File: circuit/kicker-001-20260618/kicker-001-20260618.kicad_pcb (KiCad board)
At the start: 2 copper layers, 71.4 x 59.3 mm, 60 parts, among them J1 Solenoid_{Stroke}, J2 Solenoid_{Chip}, J3 Drribler_{Front}, J4 Conn_Relay, J6 Voltmeter, Q1 BSS138, Q2 TJ15S06M3L, Q3 Q_Photo_CE, Q4 MTB010N06RJ3, Q5 MTB010N06RJ3, U1 NOT, U10 TLP2361, U11 AND, U12 AND, U2 TLP2361, U3 XL6009E1, U4 NOT, U5 NOT, U6 DRV8874, U7 NOT, U8 NOT, U9 TLP2361

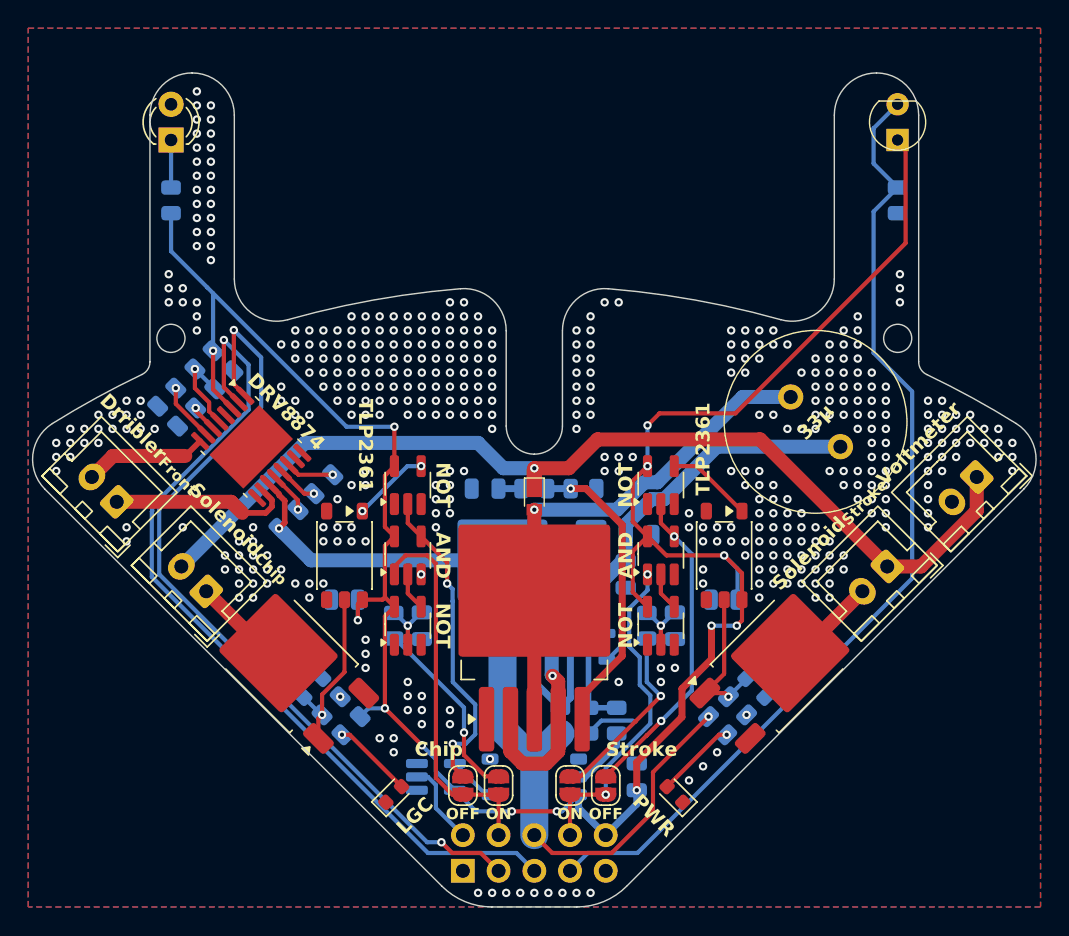
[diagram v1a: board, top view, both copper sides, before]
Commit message: Update キッカー基板のピンソケット→ピンヘッダ変更
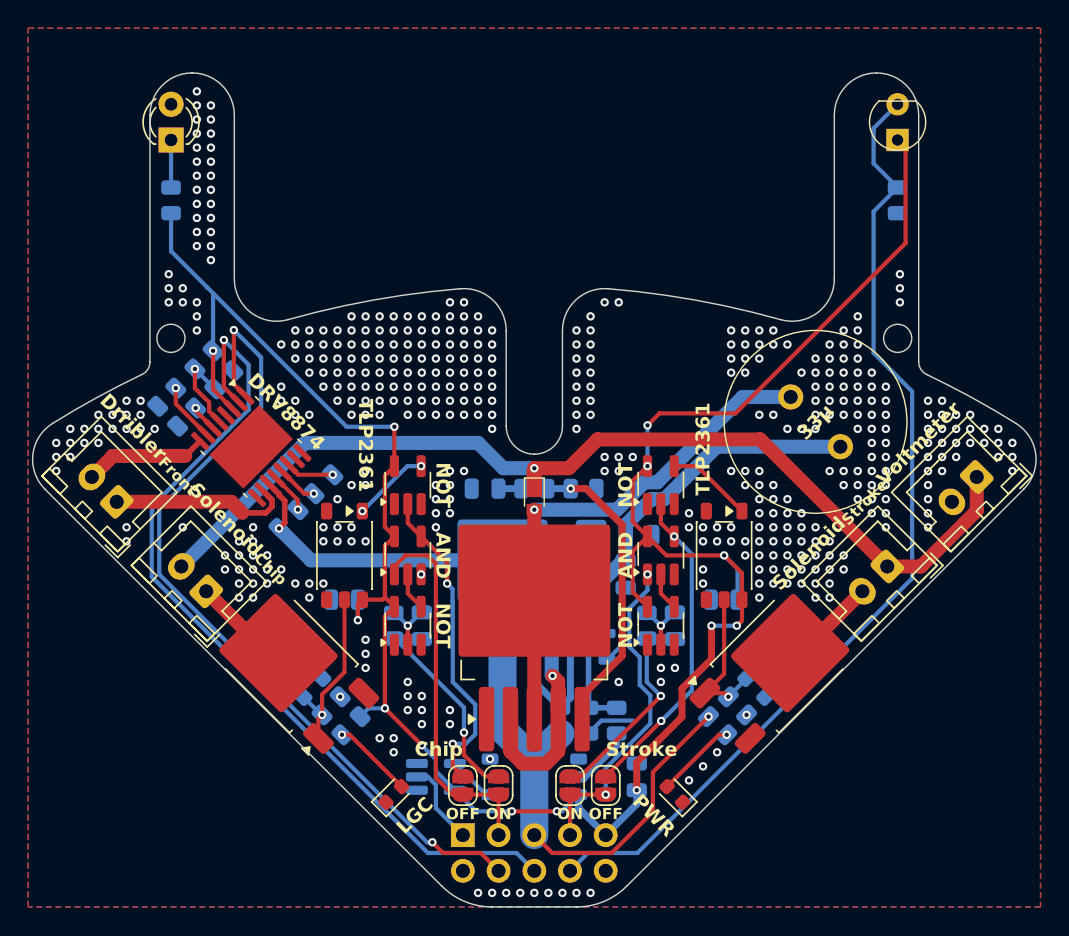
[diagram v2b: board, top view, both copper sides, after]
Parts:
- J4: footprint Connector_PinSocket_2.54mm:PinSocket_2x05_P2.54mm_Vertical -> Connector_PinHeader_2.54mm:PinHeader_2x05_P2.54mm_Vertical
- moved J4 2.54 mm to (94.9, 94.9)
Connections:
- J4 pad 1: GND -> EN_{BOOST}
- J4 pad 10: +3.3V -> GND
- J4 pad 2: EN_{BOOST} -> GND
- J4 pad 3: EN_{Dribbler-Front} -> Kick_{Chip}
- J4 pad 4: Kick_{Chip} -> EN_{Dribbler-Front}
- J4 pad 5: PH_{Dribbler-Front} -> VCC
- J4 pad 6: VCC -> PH_{Dribbler-Front}
- J4 pad 7: BallCatch_{Front} -> Kick_{Stroke}
- J4 pad 8: Kick_{Stroke} -> BallCatch_{Front}
- J4 pad 9: GND -> +3.3V
